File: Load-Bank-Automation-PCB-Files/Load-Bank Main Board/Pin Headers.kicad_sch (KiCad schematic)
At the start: 20 parts, among them J1 Conn_02x03_Counter_Clockwise, J10 Conn_02x03_Counter_Clockwise, J11 Conn_02x03_Counter_Clockwise, J12 Conn_02x03_Counter_Clockwise, J13 Conn_02x03_Counter_Clockwise, J14 Conn_02x03_Counter_Clockwise, J15 Conn_02x03_Counter_Clockwise, J16 Conn_02x03_Counter_Clockwise, J17 Conn_02x03_Counter_Clockwise, J18 Conn_02x03_Counter_Clockwise, J19 Conn_02x03_Counter_Clockwise, J20 Conn_02x03_Counter_Clockwise, J21 Conn_02x03_Counter_Clockwise, J22 Conn_02x03_Counter_Clockwise, J4 Conn_02x03_Counter_Clockwise, J5 Conn_02x03_Counter_Clockwise, J6 Conn_02x03_Counter_Clockwise, J7 Conn_02x03_Counter_Clockwise, J8 Conn_02x03_Counter_Clockwise, J9 Conn_02x03_Counter_Clockwise

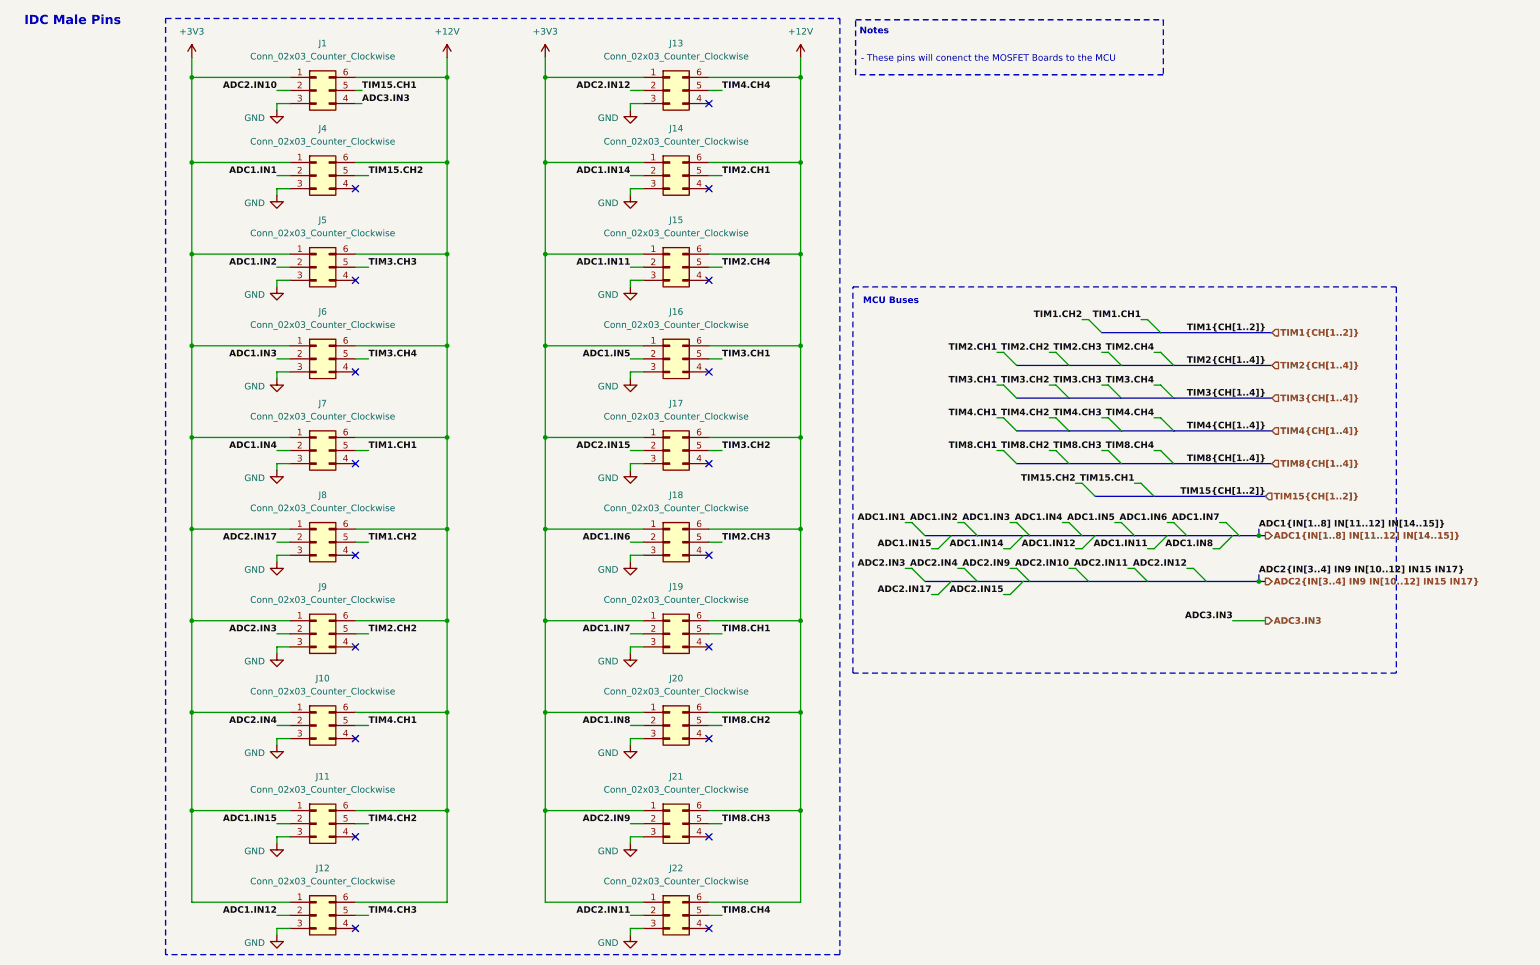
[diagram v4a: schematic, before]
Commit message: Replaced 12V-5V LDO with buck
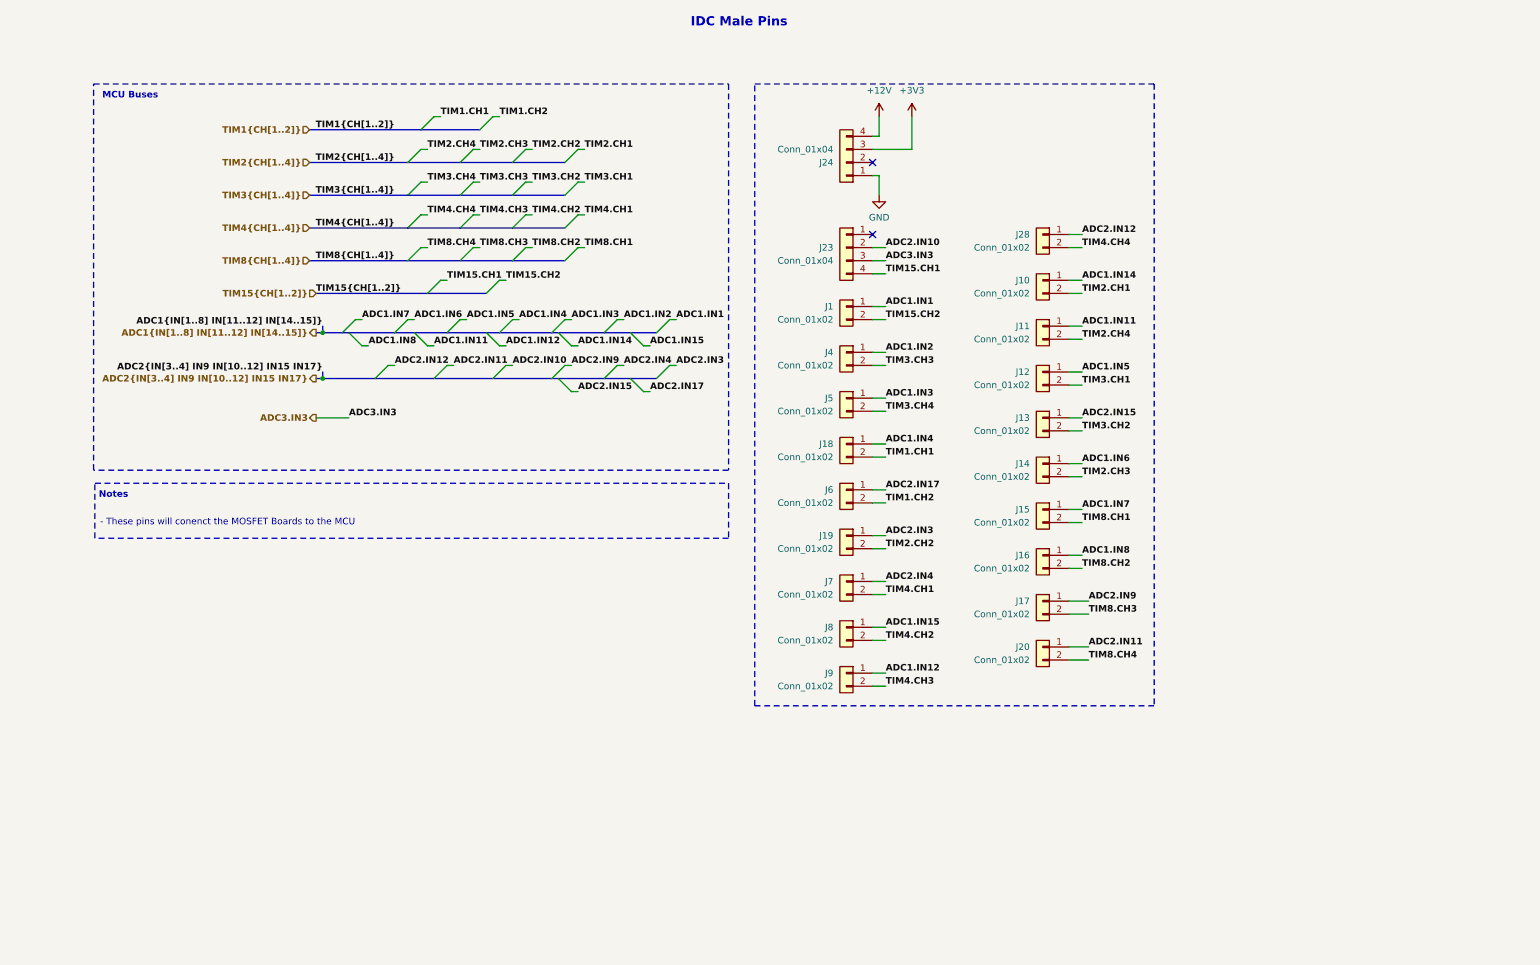
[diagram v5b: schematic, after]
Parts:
- removed J1, J10, J11, J12, J13, J14, J15, J16, J17, J18, J19, J20, J21, J22, J4, J5, J6, J7, J8, J9: Conn_02x03_Counter_Clockwise, Connector_IDC:IDC-Header_2x03_P2.54mm_Vertical, symbol Connector_Generic:Conn_02x03_Counter_Clockwise
- added J1, J10, J11, J12, J13, J14, J15, J16, J17, J18, J19, J20, J28, J4, J5, J6, J7, J8, J9: Conn_01x02, Connector_PinHeader_1.00mm:IDC_PinHeader_1x02_P1.00mm_Vertical, symbol Connector_Generic:Conn_01x02
- added J23, J24: Conn_01x04, Connector_PinHeader_1.00mm:IDC_PinHeader_1x04_P1.00mm_Vertical, symbol Connector_Generic:Conn_01x04
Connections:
- net +12V: now also J24.4 (Pin_4)
- net +3V3: now also J24.3 (Pin_3)
- net ADC1.IN1: now also J1.1 (Pin_1)
- net ADC1.IN11: now also J11.1 (Pin_1)
- net ADC1.IN12: now also J9.1 (Pin_1)
- net ADC1.IN14: now also J10.1 (Pin_1)
- net ADC1.IN15: now also J8.1 (Pin_1)
- net ADC1.IN2: now also J4.1 (Pin_1)
- net ADC1.IN3: now also J5.1 (Pin_1)
- net ADC1.IN4: now also J18.1 (Pin_1)
- net ADC1.IN5: now also J12.1 (Pin_1)
- net ADC1.IN6: now also J14.1 (Pin_1)
- net ADC1.IN7: now also J15.1 (Pin_1)
- net ADC1.IN8: now also J16.1 (Pin_1)
- net ADC2.IN10: now also J23.2 (Pin_2)
- net ADC2.IN11: now also J20.1 (Pin_1)
- net ADC2.IN12: now also J28.1 (Pin_1)
- net ADC2.IN15: now also J13.1 (Pin_1)
- net ADC2.IN17: now also J6.1 (Pin_1)
- net ADC2.IN3: now also J19.1 (Pin_1)
- net ADC2.IN4: now also J7.1 (Pin_1)
- net ADC2.IN9: now also J17.1 (Pin_1)
- net ADC3.IN3: now also J23.3 (Pin_3)
- net GND: now also J24.1 (Pin_1)
- net TIM1.CH1: now also J18.2 (Pin_2)
- net TIM1.CH2: now also J6.2 (Pin_2)
- net TIM15.CH1: now also J23.4 (Pin_4)
- net TIM15.CH2: now also J1.2 (Pin_2)
- net TIM2.CH1: now also J10.2 (Pin_2)
- net TIM2.CH2: now also J19.2 (Pin_2)
- net TIM2.CH3: now also J14.2 (Pin_2)
- net TIM2.CH4: now also J11.2 (Pin_2)
- net TIM3.CH1: now also J12.2 (Pin_2)
- net TIM3.CH2: now also J13.2 (Pin_2)
- net TIM3.CH3: now also J4.2 (Pin_2)
- net TIM3.CH4: now also J5.2 (Pin_2)
- net TIM4.CH1: now also J7.2 (Pin_2)
- net TIM4.CH2: now also J8.2 (Pin_2)
- net TIM4.CH3: now also J9.2 (Pin_2)
- net TIM4.CH4: now also J28.2 (Pin_2)
- net TIM8.CH1: now also J15.2 (Pin_2)
- net TIM8.CH2: now also J16.2 (Pin_2)
- net TIM8.CH3: now also J17.2 (Pin_2)
- net TIM8.CH4: now also J20.2 (Pin_2)
- no-connect marks 19 -> 2

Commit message: A
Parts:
- removed J23, J24: Conn_01x04, Connector_PinHeader_1.00mm:IDC_PinHeader_1x04_P1.00mm_Vertical, symbol Connector_Generic:Conn_01x04
- added J21, J22, J23: Conn_01x03, Connector_PinHeader_1.00mm:IDC_PinHeader_1x03_P1.00mm_Vertical, symbol Connector_Generic:Conn_01x03
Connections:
- net +12V: now also J21.3 (Pin_3), J22.3 (Pin_3)
- net +3V3: now also J21.2 (Pin_2), J22.2 (Pin_2)
- net ADC2.IN10: now also J23.3 (Pin_3)
- net ADC3.IN3: now also J23.2 (Pin_2)
- net GND: now also J21.1 (Pin_1), J22.1 (Pin_1)
- net TIM15.CH1: now also J23.1 (Pin_1)
- no-connect marks 2 -> 0

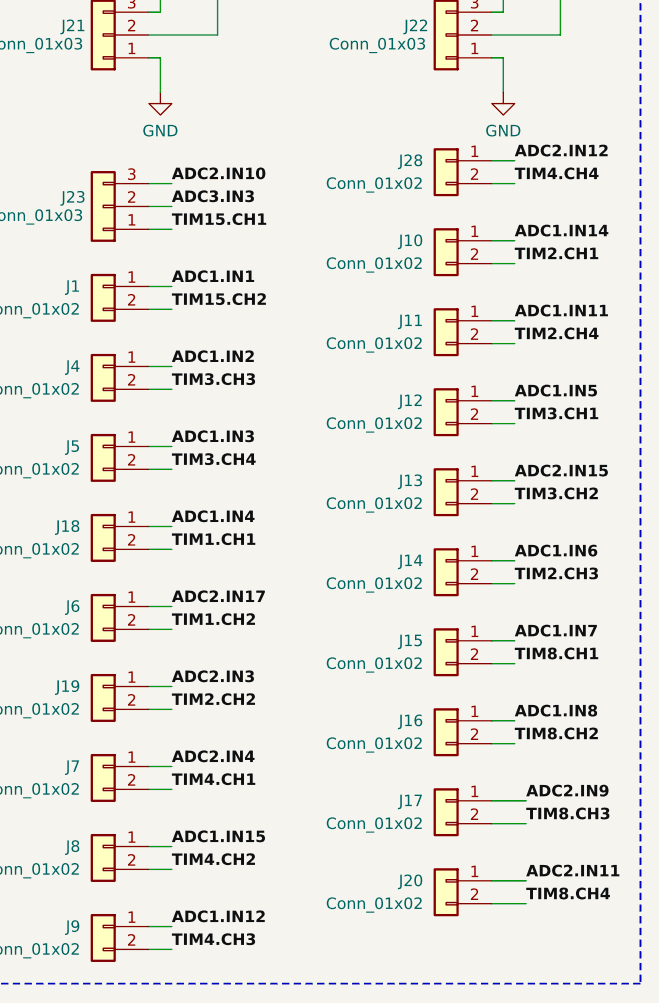
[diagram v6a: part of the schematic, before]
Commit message: All Digital Circuitry Connected
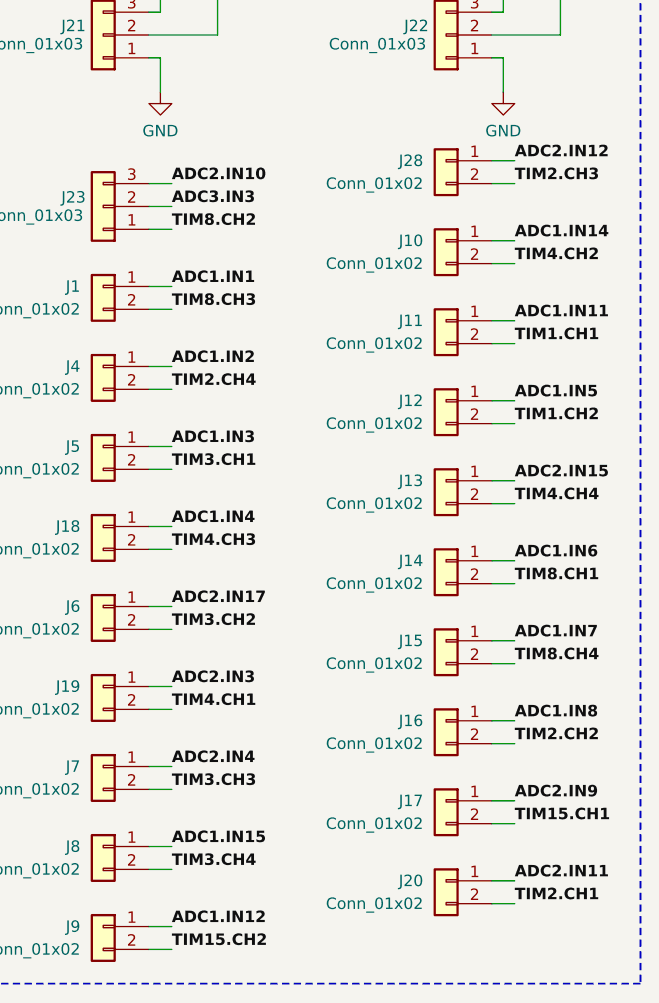
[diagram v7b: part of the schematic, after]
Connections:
- net TIM1.CH1: now also J11.2 (Pin_2); no longer J18.2 (Pin_2)
- net TIM1.CH2: now also J12.2 (Pin_2); no longer J6.2 (Pin_2)
- net TIM15.CH1: now also J17.2 (Pin_2); no longer J23.1 (Pin_1)
- net TIM15.CH2: now also J9.2 (Pin_2); no longer J1.2 (Pin_2)
- net TIM2.CH1: now also J20.2 (Pin_2); no longer J10.2 (Pin_2)
- net TIM2.CH2: now also J16.2 (Pin_2); no longer J19.2 (Pin_2)
- net TIM2.CH3: now also J28.2 (Pin_2); no longer J14.2 (Pin_2)
- net TIM2.CH4: now also J4.2 (Pin_2); no longer J11.2 (Pin_2)
- net TIM3.CH1: now also J5.2 (Pin_2); no longer J12.2 (Pin_2)
- net TIM3.CH2: now also J6.2 (Pin_2); no longer J13.2 (Pin_2)
- net TIM3.CH3: now also J7.2 (Pin_2); no longer J4.2 (Pin_2)
- net TIM3.CH4: now also J8.2 (Pin_2); no longer J5.2 (Pin_2)
- net TIM4.CH1: now also J19.2 (Pin_2); no longer J7.2 (Pin_2)
- net TIM4.CH2: now also J10.2 (Pin_2); no longer J8.2 (Pin_2)
- net TIM4.CH3: now also J18.2 (Pin_2); no longer J9.2 (Pin_2)
- net TIM4.CH4: now also J13.2 (Pin_2); no longer J28.2 (Pin_2)
- net TIM8.CH1: now also J14.2 (Pin_2); no longer J15.2 (Pin_2)
- net TIM8.CH2: now also J23.1 (Pin_1); no longer J16.2 (Pin_2)
- net TIM8.CH3: now also J1.2 (Pin_2); no longer J17.2 (Pin_2)
- net TIM8.CH4: now also J15.2 (Pin_2); no longer J20.2 (Pin_2)

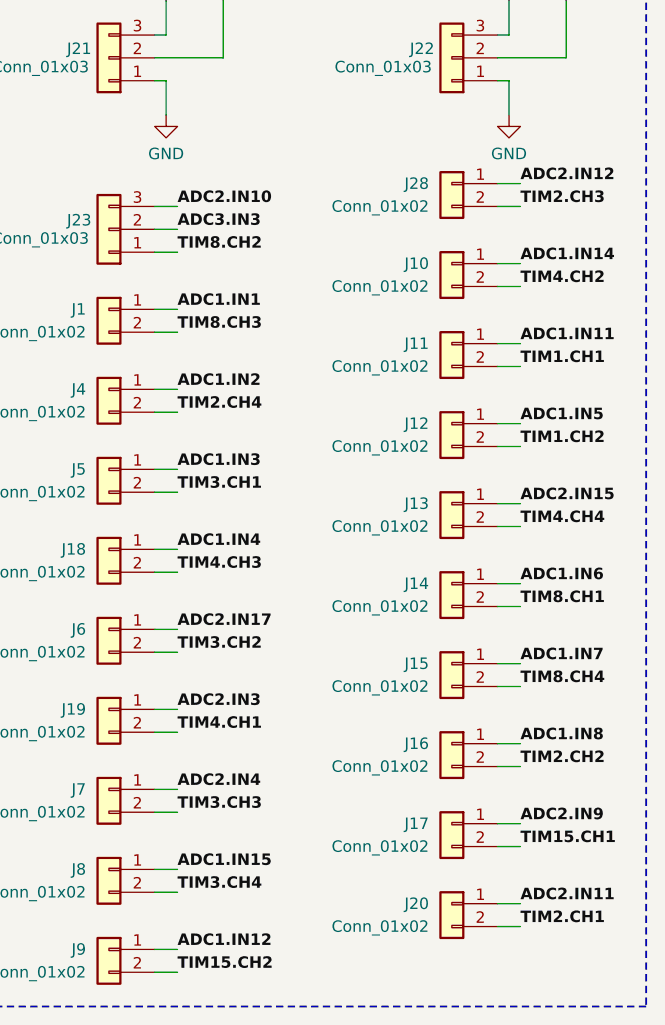
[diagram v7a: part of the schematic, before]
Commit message: Mother Board Complete. Only BOM and small silkscreen adjustments needed, other than that the board system is complete
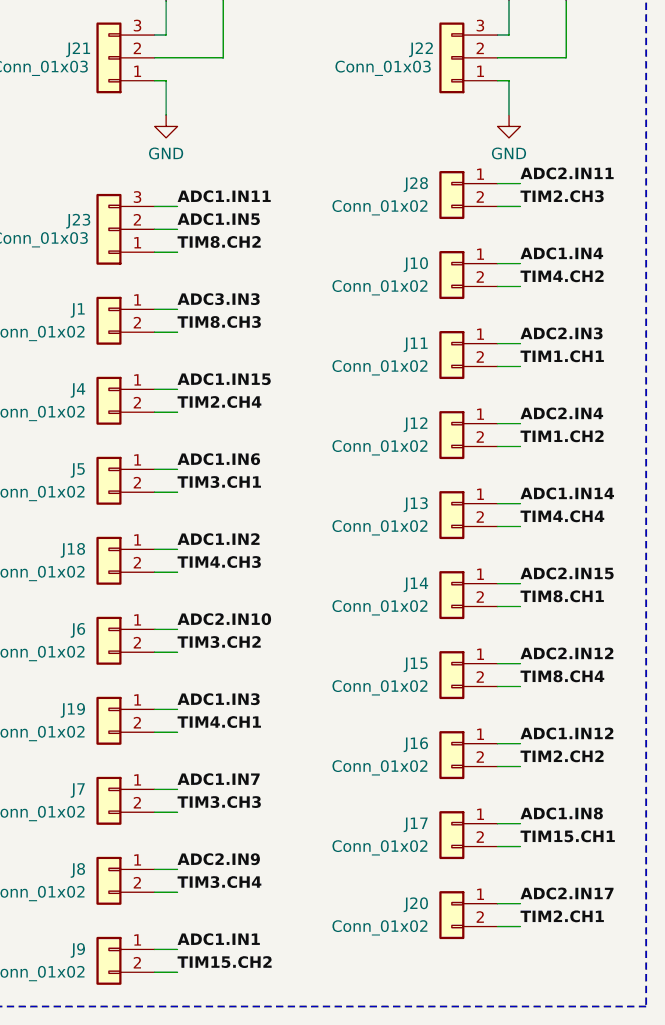
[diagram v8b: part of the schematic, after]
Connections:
- net ADC1.IN1: now also J9.1 (Pin_1); no longer J1.1 (Pin_1)
- net ADC1.IN11: now also J23.3 (Pin_3); no longer J11.1 (Pin_1)
- net ADC1.IN12: now also J16.1 (Pin_1); no longer J9.1 (Pin_1)
- net ADC1.IN14: now also J13.1 (Pin_1); no longer J10.1 (Pin_1)
- net ADC1.IN15: now also J4.1 (Pin_1); no longer J8.1 (Pin_1)
- net ADC1.IN2: now also J18.1 (Pin_1); no longer J4.1 (Pin_1)
- net ADC1.IN3: now also J19.1 (Pin_1); no longer J5.1 (Pin_1)
- net ADC1.IN4: now also J10.1 (Pin_1); no longer J18.1 (Pin_1)
- net ADC1.IN5: now also J23.2 (Pin_2); no longer J12.1 (Pin_1)
- net ADC1.IN6: now also J5.1 (Pin_1); no longer J14.1 (Pin_1)
- net ADC1.IN7: now also J7.1 (Pin_1); no longer J15.1 (Pin_1)
- net ADC1.IN8: now also J17.1 (Pin_1); no longer J16.1 (Pin_1)
- net ADC2.IN10: now also J6.1 (Pin_1); no longer J23.3 (Pin_3)
- net ADC2.IN11: now also J28.1 (Pin_1); no longer J20.1 (Pin_1)
- net ADC2.IN12: now also J15.1 (Pin_1); no longer J28.1 (Pin_1)
- net ADC2.IN15: now also J14.1 (Pin_1); no longer J13.1 (Pin_1)
- net ADC2.IN17: now also J20.1 (Pin_1); no longer J6.1 (Pin_1)
- net ADC2.IN3: now also J11.1 (Pin_1); no longer J19.1 (Pin_1)
- net ADC2.IN4: now also J12.1 (Pin_1); no longer J7.1 (Pin_1)
- net ADC2.IN9: now also J8.1 (Pin_1); no longer J17.1 (Pin_1)
- net ADC3.IN3: now also J1.1 (Pin_1); no longer J23.2 (Pin_2)
